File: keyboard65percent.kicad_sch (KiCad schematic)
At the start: 21 parts, among them J1 AVR-ISP-6, SW1 SW_SKQG, U1 ATmega32U4-A, U2 PRTR5V0U2X, X1 XTAL

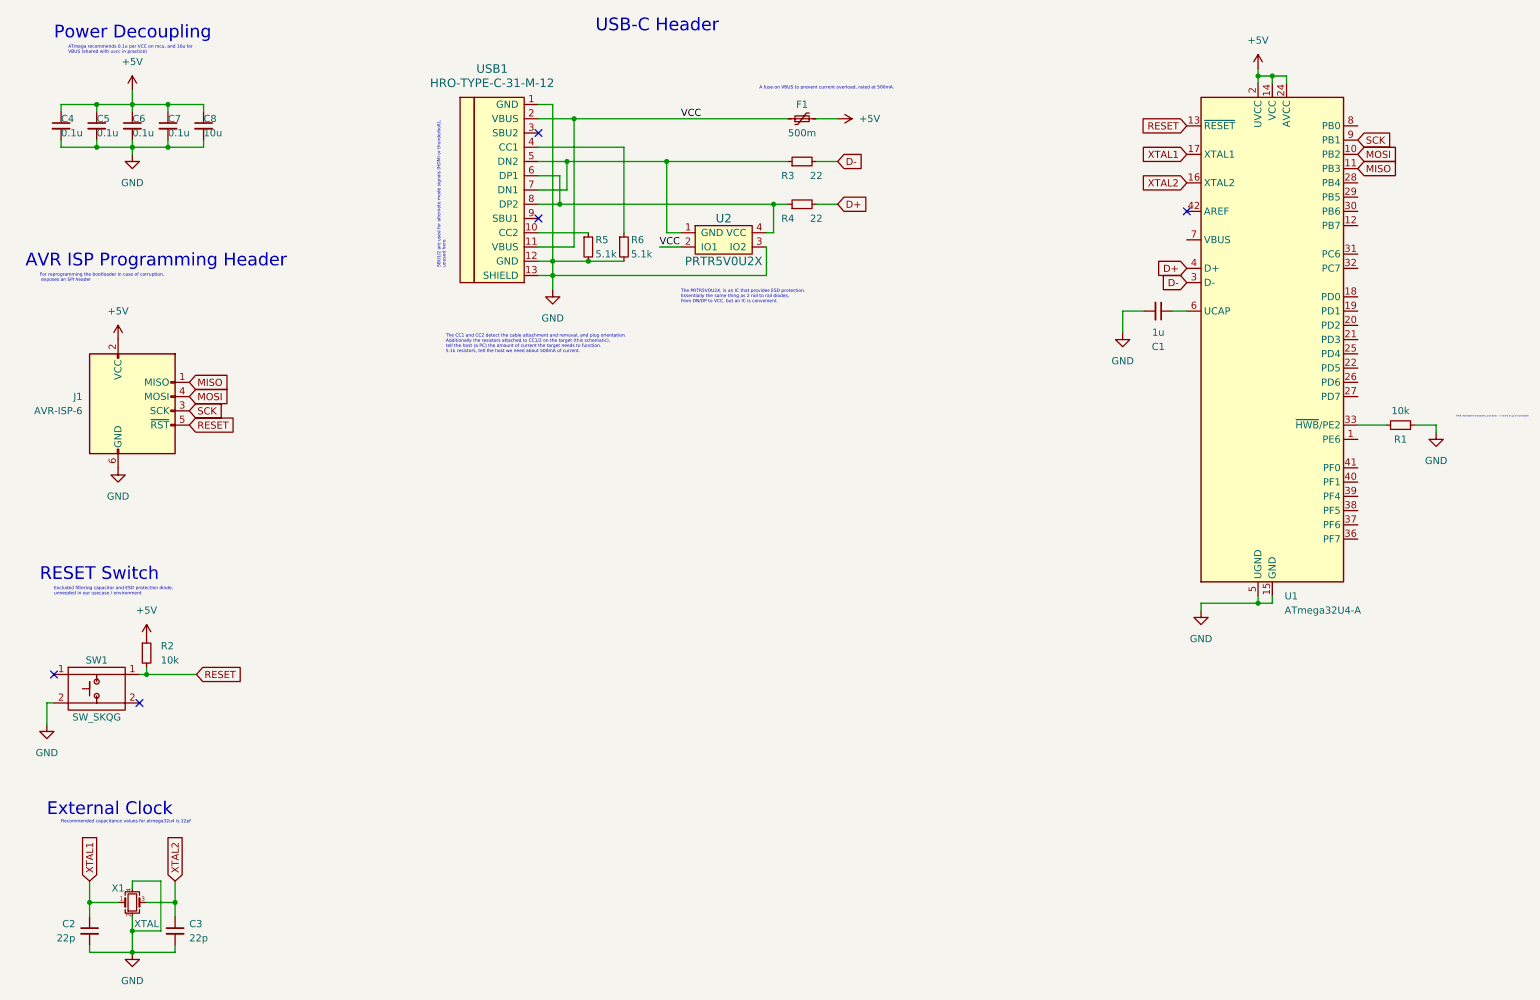
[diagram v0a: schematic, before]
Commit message: Finished schematic matrix, and footprints
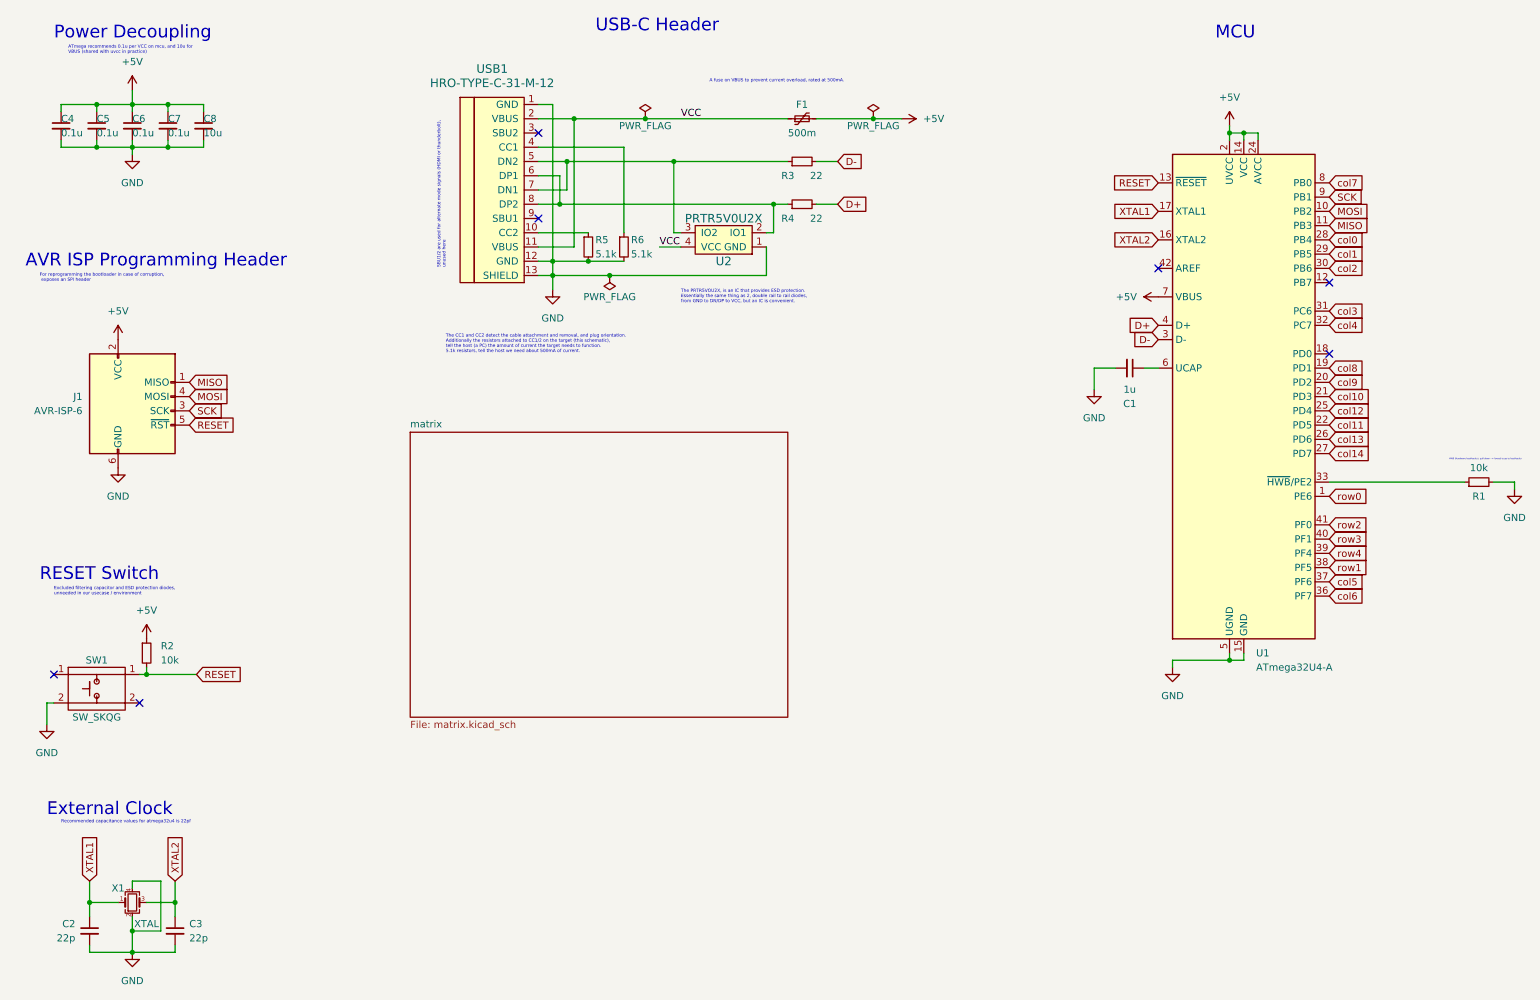
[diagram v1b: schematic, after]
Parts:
- C1, C2, C3, C4, C5, C6, C7, C8: footprint (none) -> Capacitor_SMD:C_0805_2012Metric_Pad1.18x1.45mm_HandSolder
- F1: footprint (none) -> Fuse:Fuse_1206_3216Metric_Pad1.42x1.75mm_HandSolder
- J1: footprint (none) -> random-keyboard-parts:Reset_Pretty-Mask
- R1, R2, R3, R4, R5, R6: footprint (none) -> Resistor_SMD:R_0805_2012Metric_Pad1.20x1.40mm_HandSolder
- SW1: footprint (none) -> Button_Switch_SMD:SW_SPST_SKQG_WithStem
- U2: footprint (none) -> random-keyboard-parts:SOT143B
- USB1: footprint (none) -> Type-C:HRO-TYPE-C-31-M-12-HandSoldering
- X1: footprint (none) -> Crystal:Crystal_SMD_3225-4Pin_3.2x2.5mm_HandSoldering
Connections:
- net +5V: now also U1.7 (VBUS)
- net GND: now also U2.1 (GND); no longer U2.3 (IO2)
- net VCC: now also U2.4 (VCC); no longer U2.2 (IO1)
- net at R3.1, USB1.5 (DN2), USB1.7 (DN1): now also U2.3 (IO2); no longer U2.1 (GND)
- net at R4.1, USB1.6 (DP1), USB1.8 (DP2): now also U2.2 (IO1); no longer U2.4 (VCC)
- net row0: now reaches U1.1 (PE6)
- net col8: now reaches U1.19 (PD1)
- net col9: now reaches U1.20 (PD2)
- net col10: now reaches U1.21 (PD3)
- net col11: now reaches U1.22 (PD5)
- net col12: now reaches U1.25 (PD4)
- net col13: now reaches U1.26 (PD6)
- net col14: now reaches U1.27 (PD7)
- net col0: now reaches U1.28 (PB4)
- net col1: now reaches U1.29 (PB5)
- net col2: now reaches U1.30 (PB6)
- net col3: now reaches U1.31 (PC6)
- net col4: now reaches U1.32 (PC7)
- net col6: now reaches U1.36 (PF7)
- net col5: now reaches U1.37 (PF6)
- net row1: now reaches U1.38 (PF5)
- net row4: now reaches U1.39 (PF4)
- net row3: now reaches U1.40 (PF1)
- net row2: now reaches U1.41 (PF0)
- net col7: now reaches U1.8 (PB0)
- no-connect marks 5 -> 7
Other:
- added sheet matrix (matrix.kicad_sch)
- note added: "Excluded filtering capacitor and ESD protection diodes, unneeded in our usecase / environment"
- note added: "MCU"
- note added: "The PRTR5VOU2X, is an IC that provides ESD protection. Essentially the same thing as 2, double rail to rail diodes, from GND to DN/DP to VCC, but an IC is convenient."
- note removed: "Excluded filtering capacitor and ESD protection diode, unneeded in our usecase / environment"
- note removed: "The PRTR5VOU2X, is an IC that provides ESD protection. Essentially the same thing as 2 rail to rail diodes, from DN/DP to VCC, but an IC is convenient."
- moved on the sheet: C1, R1, U1, U2
